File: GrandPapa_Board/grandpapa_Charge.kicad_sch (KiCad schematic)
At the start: 25 parts, among them J1 3.7V LiPo Single Cell, J8 Therm EN Jumper, U3 MCP73871T-1CCI/ML, U4 INA180

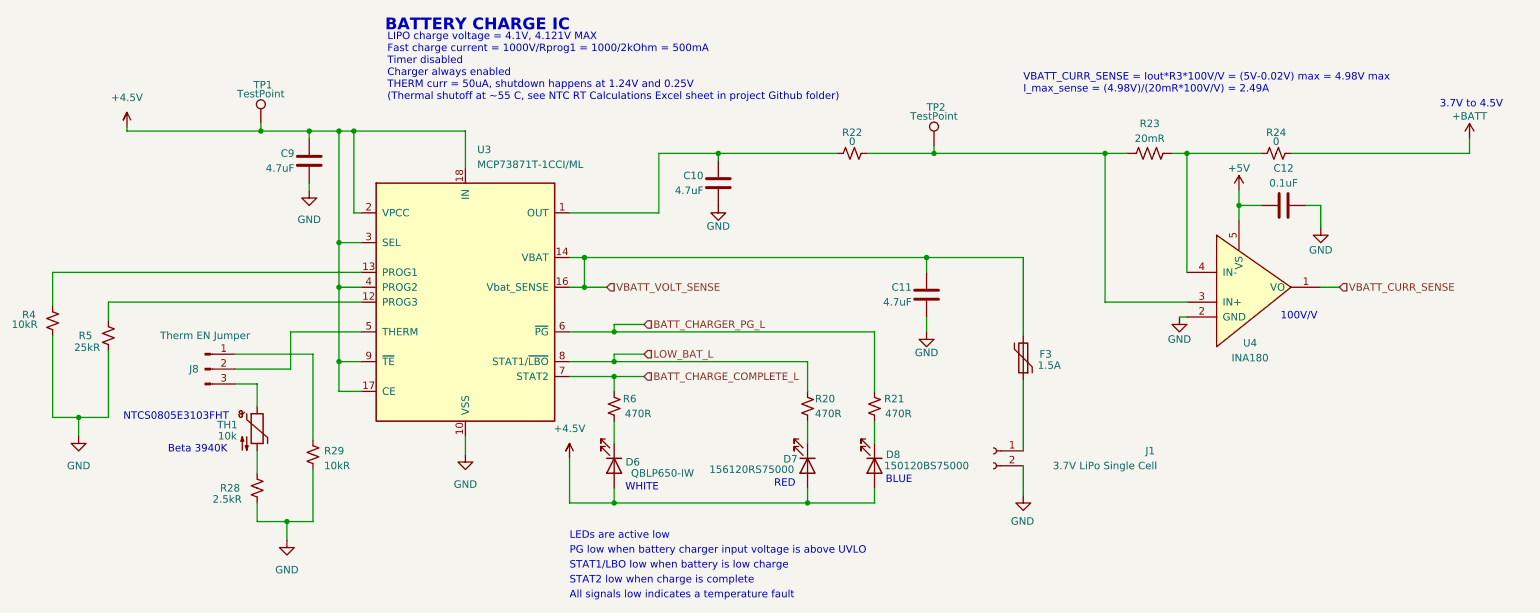
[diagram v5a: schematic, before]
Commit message: fix charging prog1 resistor value, fix schematic grid
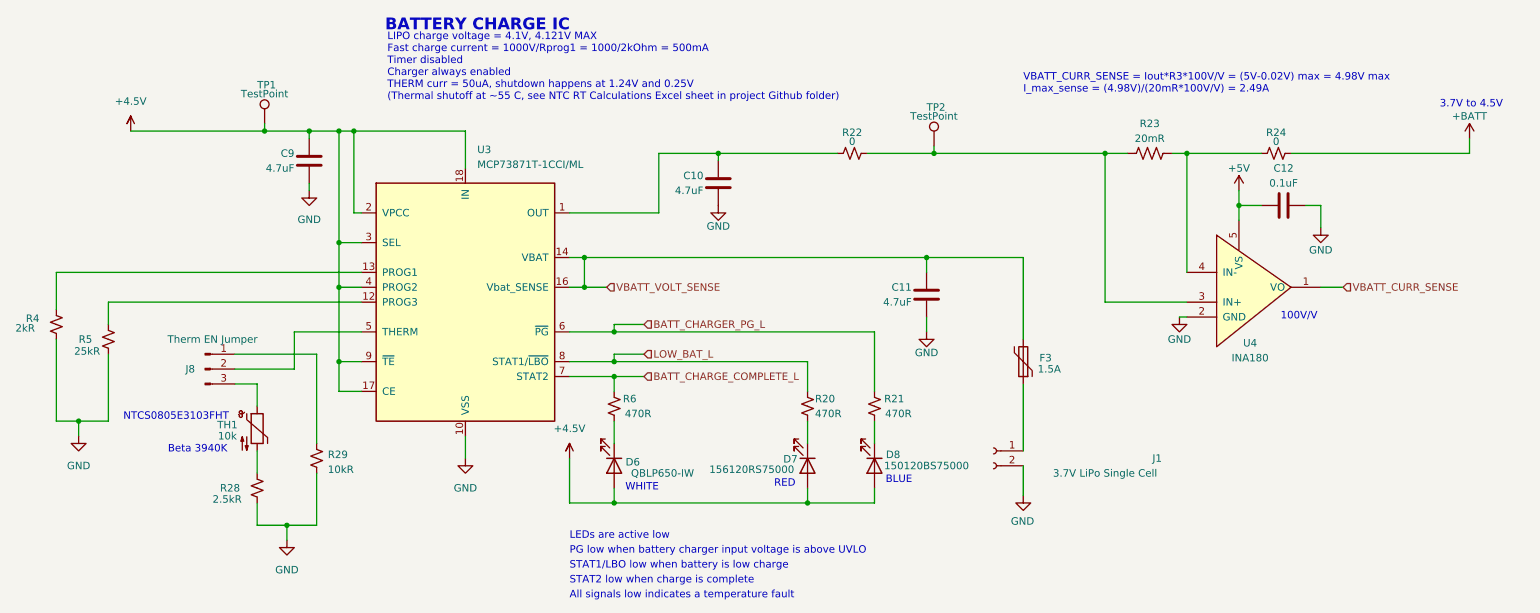
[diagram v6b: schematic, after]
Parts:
- removed J1: 3.7V LiPo Single Cell, Connector_JST:JST_PH_S2B-PH-K_1x02_P2.00mm_Horizontal, symbol Connector:Conn_01x02_Female
- removed J8: Therm EN Jumper, Connector_PinHeader_2.54mm:PinHeader_1x03_P2.54mm_Vertical, symbol Connector:Conn_01x03_Male
- added J1: 3.7V LiPo Single Cell, symbol Connector:Conn_01x02_Socket
- added J8: Therm EN Jumper, symbol Connector:Conn_01x03_Pin
- R4: value 10kR -> 2kR
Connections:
- net GND: now also J1.2 (Pin_2)
- net at R29.1: now also J8.1 (Pin_1)
- net at U3.5 (THERM): now also J8.2 (Pin_2)
- net at TH1.1: now also J8.3 (Pin_3)
- net at F3.1: now also J1.1 (Pin_1)
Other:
- moved on the sheet: F3, R29, R4, R5, TP1
